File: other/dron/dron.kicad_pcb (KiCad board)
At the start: 2 copper layers, 84.2 x 84.2 mm, 7 parts, among them J1 DCV, J2 ESC1, J3 ESC2, J4 ESC3, J5 ESC4, J6 BAT

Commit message: complete motor holes for dron
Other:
- outline, holes or cut-outs redrawn
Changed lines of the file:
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@@
+		(layer "Edge.Cuts")
+	)
+	(gr_circle
+		(center 131.1402 127.8128)
+		(end 132.0038 127.8128)
+		(stroke
+			(width 0.05)
+			(type default)
+		)
+		(fill none)
 		(layer "Edge.Cuts")
 	)
@@
 		(layer "Edge.Cuts")
 	)
+	(gr_circle
+		(center 133.6294 129.6162)
+		(end 134.3914 129.6162)
+		(stroke
+			(width 0.05)
+			(type default)
+		)
+		(fill none)
+		(layer "Edge.Cuts")
+	)
 	(gr_line
 		(start 102.997 110.236)
@@
 			(type default)
 		)
+		(layer "Edge.Cuts")
+	)
+	(gr_circle
+		(center 55.8038 59.182)
+		(end 56.6674 59.182)
+		(stroke
+			(width 0.05)
+			(type default)
+		)
+		(fill none)
+		(layer "Edge.Cuts")
+	)
+	(gr_circle
+		(center 55.8038 127.8128)
+		(end 56.6674 127.8128)
+		(stroke
+			(width 0.05)
+			(type default)
+		)
+		(fill none)
 		(layer "Edge.Cuts")
 	)
@@
 		(layer "Edge.Cuts")
 	)
+	(gr_circle
+		(center 133.6294 57.3786)
+		(end 134.3914 57.3786)
+		(stroke
+			(width 0.05)
+			(type default)
+		)
+		(fill none)
+		(layer "Edge.Cuts")
+	)
 	(gr_arc
 		(start 57.277 61.595)
@@
 		(layer "Edge.Cuts")
 	)
+	(gr_circle
+		(center 127.762 55.8038)
+		(end 128.6256 55.8038)
+		(stroke
+			(width 0.05)
+			(type default)
+		)
+		(fill none)
+		(layer "Edge.Cuts")
+	)
 	(gr_line
 		(start 105.044408 76.692592)
@@
 		(center 132.3848 132.4356)
 		(end 133.2484 132.4356)
+		(stroke
+			(width 0.05)
+			(type default)
+		)
+		(fill none)
+		(layer "Edge.Cuts")
+	)
+	(gr_circle
+		(center 59.182 131.191)
+		(end 60.0456 131.191)
 		(stroke
 			(width 0.05)
@@
 		(layer "Edge.Cuts")
 	)
+	(gr_circle
+		(center 53.3146 57.3786)
+		(end 54.0766 57.3786)
+		(stroke
+			(width 0.05)
+			(type default)
+		)
+		(fill none)
+		(layer "Edge.Cuts")
+	)
 	(gr_line
 		(start 67.818 123.444)
@@
 	)
 	(gr_circle
+		(center 129.5654 133.6802)
+		(end 130.3274 133.6802)
+		(stroke
+			(width 0.05)
+			(type default)
+		)
+		(fill none)
+		(layer "Edge.Cuts")
+	)
+	(gr_circle
 		(center 58.8518 58.8518)
 		(end 59.6138 58.8518)
@@
 		(layer "Edge.Cuts")
 	)
+	(gr_circle
+		(center 127.762 131.191)
+		(end 128.6256 131.191)
+		(stroke
+			(width 0.05)
+			(type default)
+		)
+		(fill none)
+		(layer "Edge.Cuts")
+	)
 	(gr_line
 		(start 63.5 119.126)
@@
 		(layer "Edge.Cuts")
 	)
+	(gr_circle
+		(center 129.5654 53.3146)
+		(end 130.3274 53.3146)
+		(stroke
+			(width 0.05)
+			(type default)
+		)
+		(fill none)
+		(layer "Edge.Cuts")
+	)
 	(gr_line
 		(start 123.444 119.126)
@@
 			(type default)
 		)
+		(layer "Edge.Cuts")
+	)
+	(gr_circle
+		(center 59.182 55.8038)
+		(end 60.0456 55.8038)
+		(stroke
+			(width 0.05)
+			(type default)
+		)
+		(fill none)
+		(layer "Edge.Cuts")
+	)
+	(gr_circle
+		(center 57.3786 133.6802)
+		(end 58.1406 133.6802)
+		(stroke
+			(width 0.05)
+			(type default)
+		)
+		(fill none)
 		(layer "Edge.Cuts")
 	)
@@
 		(layer "Edge.Cuts")
 	)
+	(gr_circle
+		(center 57.3786 53.3146)
+		(end 58.1406 53.3146)
+		(stroke
+			(width 0.05)
+			(type default)
+		)
+		(fill none)
+		(layer "Edge.Cuts")
+	)
 	(gr_line
 		(start 81.915 110.236)
@@
 		(layer "Edge.Cuts")
 	)
+	(gr_circle
+		(center 131.1402 59.182)
+		(end 132.0038 59.182)
+		(stroke
+			(width 0.05)
+			(type default)
+		)
+		(fill none)
+		(layer "Edge.Cuts")
+	)
 	(gr_line
 		(start 81.915 81.899592)
@@
 		(layer "Edge.Cuts")
 	)
+	(gr_circle
+		(center 53.3146 129.6162)
+		(end 54.0766 129.6162)
+		(stroke
+			(width 0.05)
+			(type default)
+		)
+		(fill none)
+		(layer "Edge.Cuts")
+	)

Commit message: add dron author and J-logo to RTC-SD
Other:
- board text added: "@pinchito"
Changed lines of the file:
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@@
 		(layer "Edge.Cuts")
+	)
+	(gr_text "@pinchito"
+		(at 105.41 69.85 0)
+		(layer "B.SilkS")
+		(effects
+			(font
+				(size 2 2)
+				(thickness 0.32)
+			)
+			(justify left bottom mirror)
+		)
 	)
 	(gr_text "Avis Quaterna"

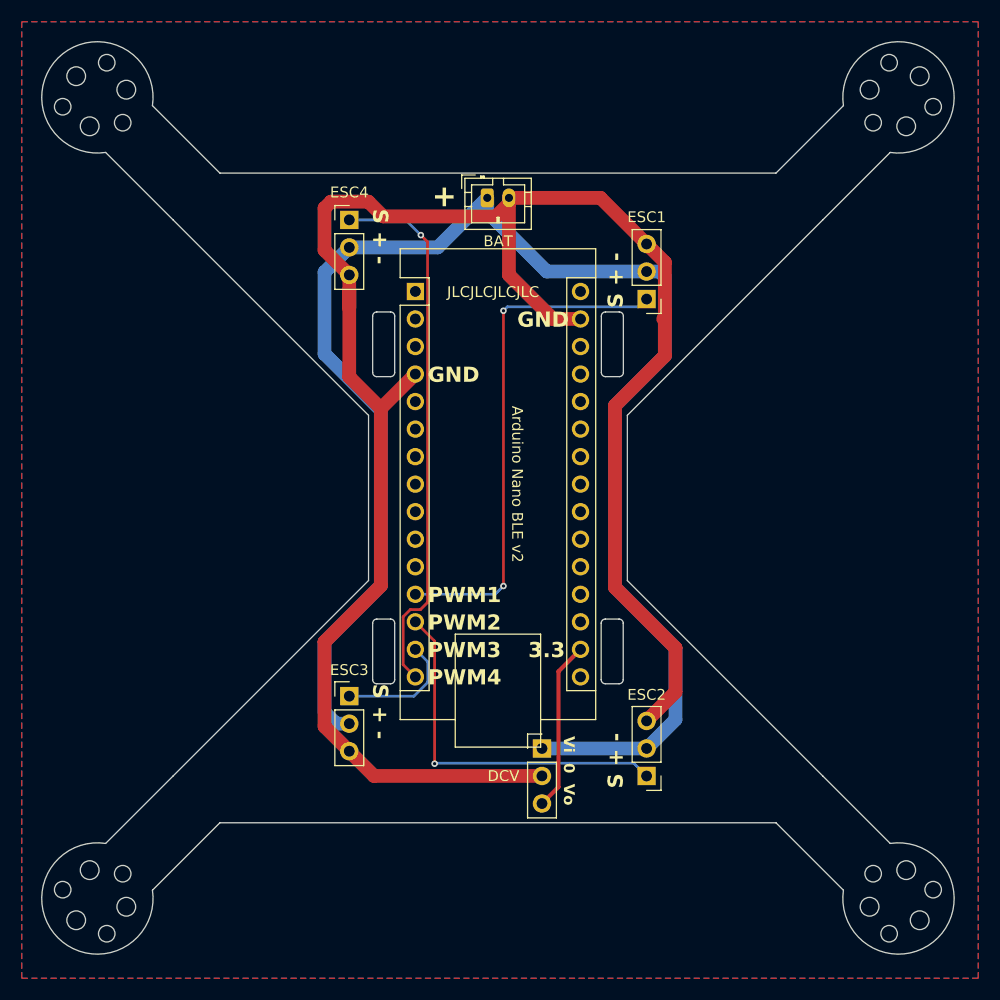
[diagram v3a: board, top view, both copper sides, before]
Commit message: reduce axle hole
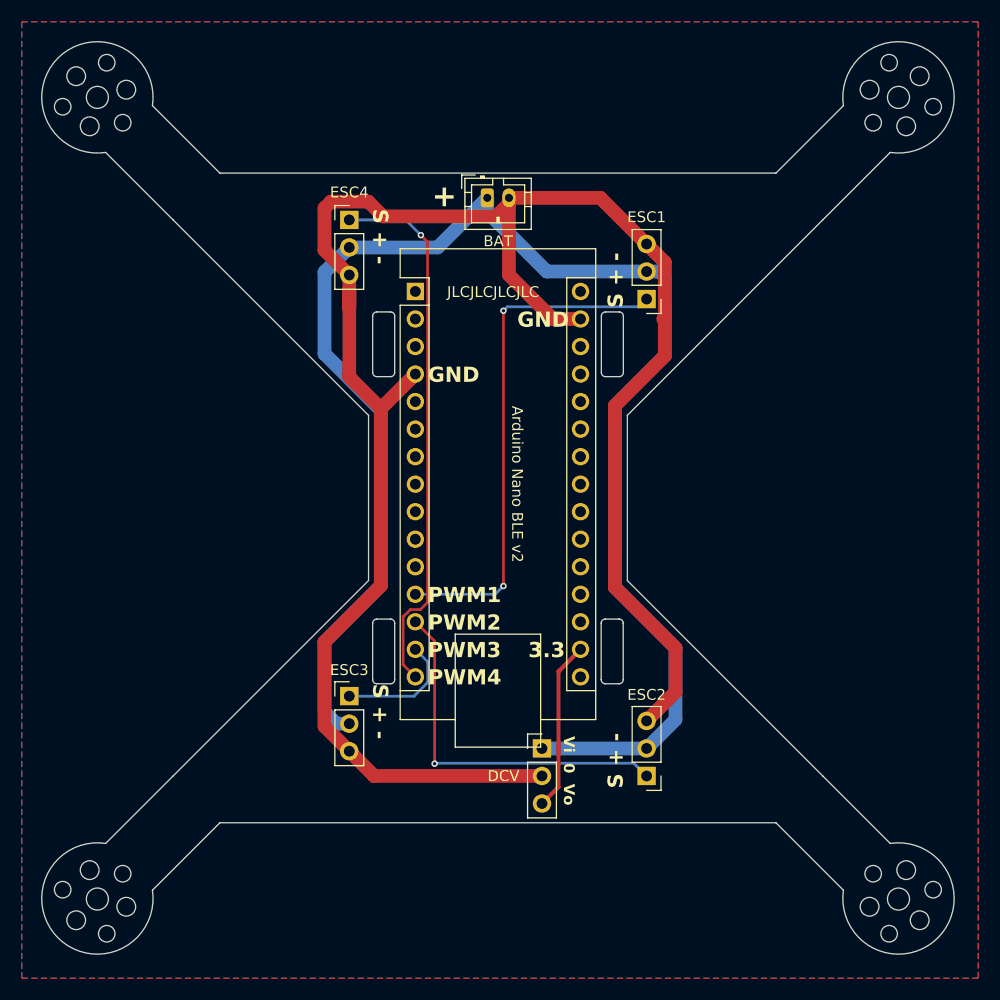
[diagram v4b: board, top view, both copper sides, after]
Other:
- outline, holes or cut-outs redrawn
- board text removed: "@pinchito"
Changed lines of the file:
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@@
+	)
+	(gr_circle
+		(center 130.429 130.4798)
+		(end 131.445 130.4798)
+		(stroke
+			(width 0.05)
+			(type default)
+		)
+		(fill none)
+		(layer "Edge.Cuts")
 	)
 	(gr_circle
@@
 		(layer "Edge.Cuts")
 	)
+	(gr_circle
+		(center 130.429 56.515)
+		(end 131.445 56.515)
+		(stroke
+			(width 0.05)
+			(type default)
+		)
+		(fill none)
+		(layer "Edge.Cuts")
+	)
+	(gr_circle
+		(center 56.515 130.4798)
+		(end 57.531 130.4798)
+		(stroke
+			(width 0.05)
+			(type default)
+		)
+		(fill none)
+		(layer "Edge.Cuts")
+	)
 	(gr_line
 		(start 105.044408 76.692592)
@@
 		(layer "Edge.Cuts")
 	)
+	(gr_circle
+		(center 56.515 56.515)
+		(end 57.531 56.515)
+		(stroke
+			(width 0.05)
+			(type default)
+		)
+		(fill none)
+		(layer "Edge.Cuts")
+	)
 	(gr_line
 		(start 67.818 123.444)
@@
 		(layer "Edge.Cuts")
 	)
-	(gr_text "@pinchito"
-		(at 105.41 69.85 0)
-		(layer "B.SilkS")
-		(effects
-			(font
-				(size 2 2)
-				(thickness 0.32)
-			)
-			(justify left bottom mirror)
-		)
-	)
 	(gr_text "Avis Quaterna"
